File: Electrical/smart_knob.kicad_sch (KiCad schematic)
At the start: 75 parts, among them J1 Conn_01x04_Male, J2 USB_C_Receptacle_USB2.0, J3 Conn_01x08_Male, J4 Conn_01x03_Male, J5 Barrel_Jack_Switch, SW1 SW_SPDT, U1 DRV8311H, U2 LD3985M33R_SOT23, U3 TXU0101, U4 TLV493D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

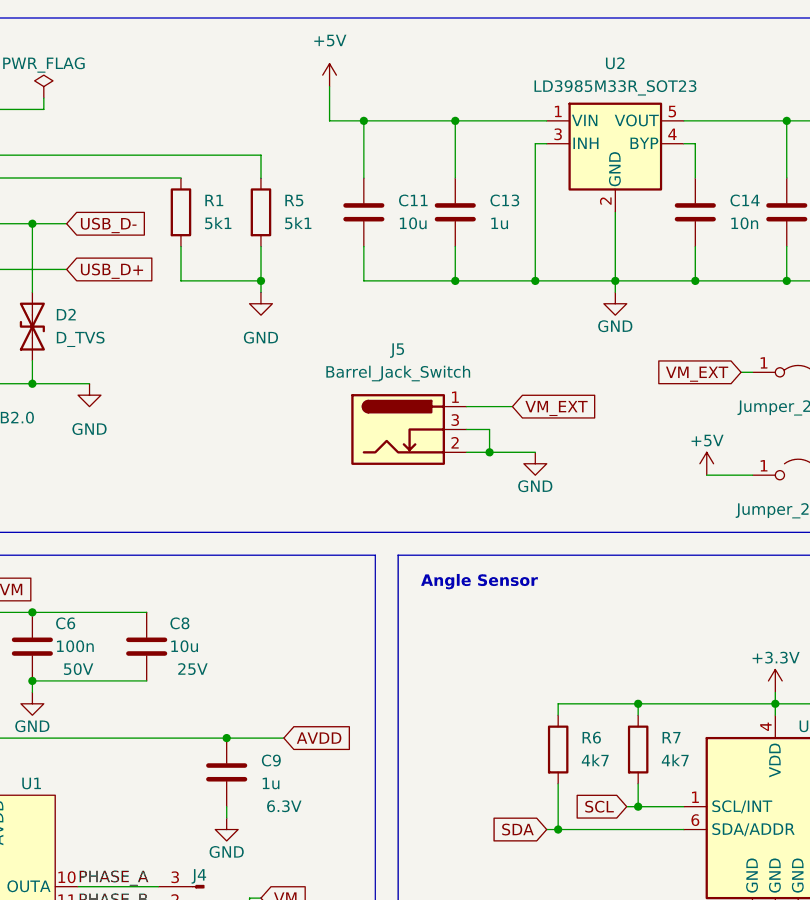
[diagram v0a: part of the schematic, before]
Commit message: fix schematic rework issues
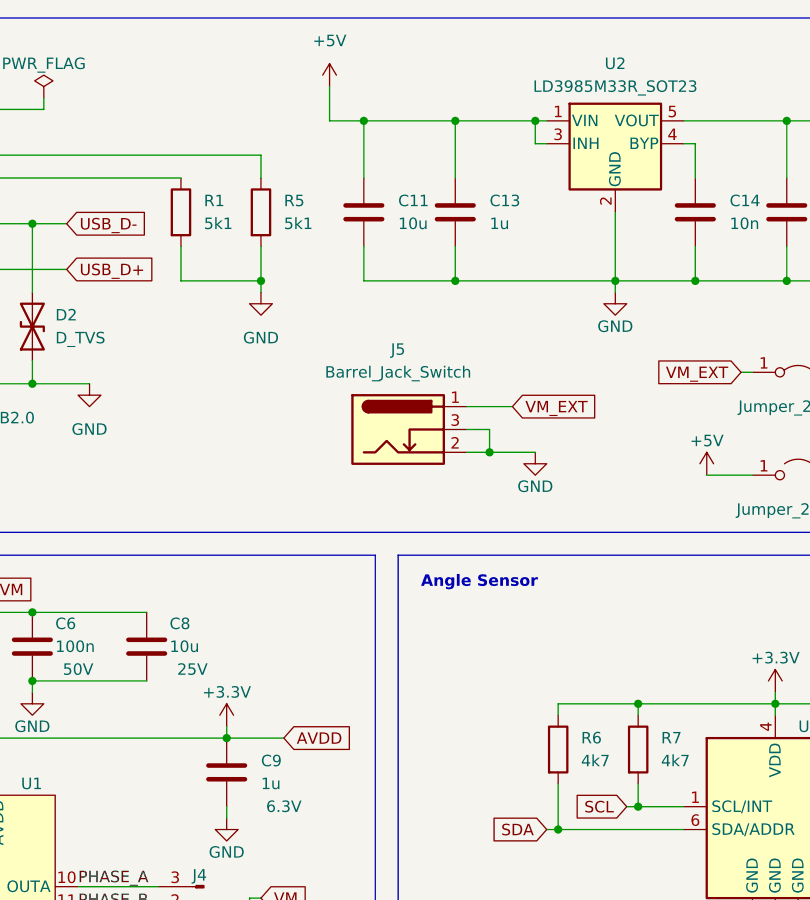
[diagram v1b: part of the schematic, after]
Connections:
- net AVDD is gone; now on net +3.3V: C9.1, R2.2, U1.17 (AVDD), U1.22 (SLEW), U1.24 (nSLEEP)
- net +5V: now also U2.3 (INH)
- net GND: no longer U2.3 (INH)
